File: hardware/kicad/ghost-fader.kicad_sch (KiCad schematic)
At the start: 0 parts

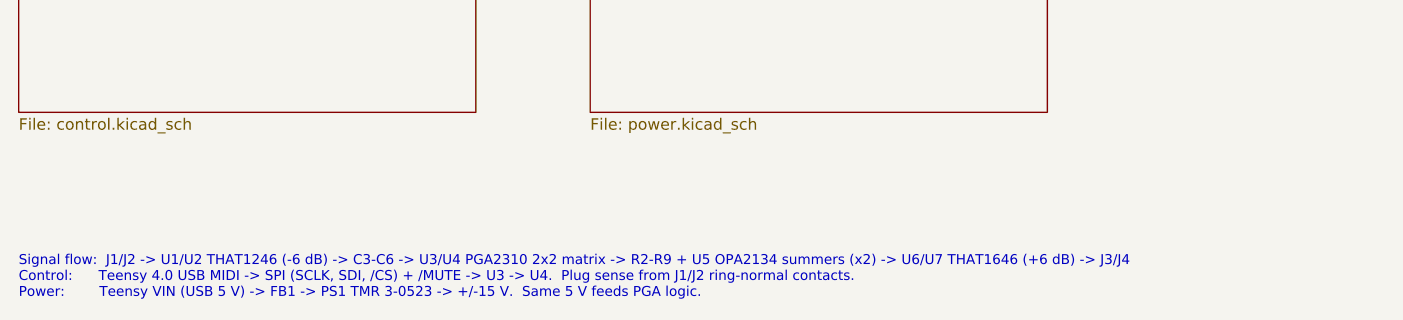
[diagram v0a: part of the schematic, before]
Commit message: Rev C: XIAO RP2040 and Traco TBA 2-0522 replace the Teensy 4.0 and TMR 3
Tier 1 cost-down, no change to the audio path. U9 becomes a Seeed XIAO
RP2040 on header pins (USB-C, TinyUSB MIDI, its 5V pin is VBUS straight
through), PS1 becomes a 2 W unregulated Traco TBA 2-0522 on KiCad's stock
SIP-7 footprint. Rails are now +/-12 V: the +/-15 V TBA 2-0523 would pass
the PGA2310's 16 V absolute maximum at light load. Parts cost drops from
about $145 to about $110.

- gen.py: TBA2_Dual and XIAO_RP2040 symbols, XIAO footprint (Seeed pin
  numbering, USB-C overhang drawn), control sheet rewired to D0-D10,
  power sheet and notes for the unregulated converter, +/-12V rails.
- check.py: new U9 / PS1 pins; NETLIST OK. ERC 0/0.
- Both boards rebuilt and re-routed (Freerouting 1.9), DRC 0 errors; the
  only warnings are jack-nose and USB-C shell silk over the board edge.
- Gerbers, drill, zips, BOM, schematic SVG/PDF and board renders
  regenerated. README and site updated: pin map, power budget
  (~250 mA typical), level budget at +/-12 V, parts list and totals.

Co-Authored-By: Claude Fable 5.1 <noreply@anthropic.com>
Claude-Session: https://claude.ai/code/session_01C8uqpe49go1TPWMsWKKVkn
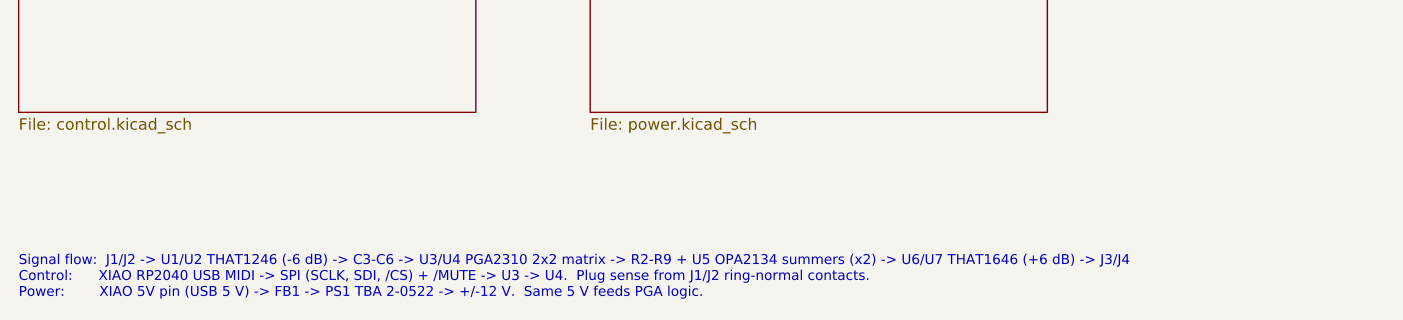
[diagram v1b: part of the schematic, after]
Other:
- note added: "Signal flow: J1/J2 -> U1/U2 THAT1246 (-6 dB) -> C3-C6 -> U3/U4 PGA2310 2x2 matrix -> R2-R9 + U5 OPA2134 summers (x2) -> U6/U7 THAT1646 (+6 dB) -> J3/J4 Control: XIAO RP2040 USB MIDI -> SPI (SCLK, SDI, /CS) + /MUTE -> U3 -> U4. Plug sense from J1/J2 ring-normal contacts. Power: XIAO 5V pin (USB 5 V) -> FB1 -> PS1 TBA 2-0522 -> +/-12 V. Same 5 V feeds PGA logic."
- note removed: "Signal flow: J1/J2 -> U1/U2 THAT1246 (-6 dB) -> C3-C6 -> U3/U4 PGA2310 2x2 matrix -> R2-R9 + U5 OPA2134 summers (x2) -> U6/U7 THAT1646 (+6 dB) -> J3/J4 Control: Teensy 4.0 USB MIDI -> SPI (SCLK, SDI, /CS) + /MUTE -> U3 -> U4. Plug sense from J1/J2 ring-normal contacts. Power: Teensy VIN (USB 5 V) -> FB1 -> PS1 TMR 3-0523 -> +/-15 V. Same 5 V feeds PGA logic."
- title: Ghost Fader - Rev B -> Ghost Fader - Rev C
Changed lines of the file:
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@@
 (kicad_sch (version 20250114) (generator "ghost-fader-gen") (generator_version "9.0") (paper "A4")
-  (title_block (title "Ghost Fader - Rev B") (date "2026-09-06") (rev "B") (company "Ghost Fader") (comment 1 "USB-MIDI volume and pan for two balanced line channels") (comment 2 "https://chris-albert.github.io/ghost-fader/"))
+  (title_block (title "Ghost Fader - Rev C") (date "2026-09-08") (rev "C") (company "Ghost Fader") (comment 1 "USB-MIDI volume and pan for two balanced line channels") (comment 2 "https://chris-albert.github.io/ghost-fader/"))
   (text "Ghost Fader" (exclude_from_sim no) (at 25.4 33.02 0) (effects (font (size 3.5 3.5)) (justify left bottom)))
   (text "USB-MIDI-controlled volume and pan for two balanced 1/4\" line channels. Bus powered, no external supply.\nSheets: 1 input, 2 matrix, 3 output, 4 control, 5 power. Nets between sheets are global labels; rails are power symbols." (exclude_from_sim no) (at 25.4 40.64 0) (effects (font (size 1.27 1.27)) (justify left bottom)))
@@
     (property "Sheetname" "Balanced inputs" (at 25.4 55.18 0) (effects (font (size 1.27 1.27)) (justify left bottom)))
     (property "Sheetfile" "input.kicad_sch" (at 25.4 76.8 0) (effects (font (size 1.27 1.27)) (justify left top)))
-    (instances (project "ghost-fader" (path "/fea7b9ca-c814-4436-8b9b-27ea79511ff8" (page "2"))))
+    (instances (project "ghost-fader" (path "/4c5c562c-d270-4690-8736-07f5ac58d31a" (page "2"))))
   )
   (sheet (at 88.9 55.88) (size 50.8 20.32) (exclude_from_sim no) (in_bom yes) (on_board yes) (dnp no) (fields_autoplaced yes) (stroke (width 0.1524) (type solid)) (fill (color 0 0 0 0.0000))
     (property "Sheetname" "2x2 gain matrix and summers" (at 88.9 55.18 0) (effects (font (size 1.27 1.27)) (justify left bottom)))
     (property "Sheetfile" "matrix.kicad_sch" (at 88.9 76.8 0) (effects (font (size 1.27 1.27)) (justify left top)))
-    (instances (project "ghost-fader" (path "/fea7b9ca-c814-4436-8b9b-27ea79511ff8" (page "3"))))
+    (instances (project "ghost-fader" (path "/4c5c562c-d270-4690-8736-07f5ac58d31a" (page "3"))))
   )
   (sheet (at 152.4 55.88) (size 50.8 20.32) (exclude_from_sim no) (in_bom yes) (on_board yes) (dnp no) (fields_autoplaced yes) (stroke (width 0.1524) (type solid)) (fill (color 0 0 0 0.0000))
     (property "Sheetname" "Balanced outputs" (at 152.4 55.18 0) (effects (font (size 1.27 1.27)) (justify left bottom)))
     (property "Sheetfile" "output.kicad_sch" (at 152.4 76.8 0) (effects (font (size 1.27 1.27)) (justify left top)))
-    (instances (project "ghost-fader" (path "/fea7b9ca-c814-4436-8b9b-27ea79511ff8" (page "4"))))
+    (instances (project "ghost-fader" (path "/4c5c562c-d270-4690-8736-07f5ac58d31a" (page "4"))))
   )
   (sheet (at 25.4 88.9) (size 50.8 20.32) (exclude_from_sim no) (in_bom yes) (on_board yes) (dnp no) (fields_autoplaced yes) (stroke (width 0.1524) (type solid)) (fill (color 0 0 0 0.0000))
     (property "Sheetname" "Control" (at 25.4 88.2 0) (effects (font (size 1.27 1.27)) (justify left bottom)))
     (property "Sheetfile" "control.kicad_sch" (at 25.4 109.82 0) (effects (font (size 1.27 1.27)) (justify left top)))
-    (instances (project "ghost-fader" (path "/fea7b9ca-c814-4436-8b9b-27ea79511ff8" (page "5"))))
+    (instances (project "ghost-fader" (path "/4c5c562c-d270-4690-8736-07f5ac58d31a" (page "5"))))
   )
   (sheet (at 88.9 88.9) (size 50.8 20.32) (exclude_from_sim no) (in_bom yes) (on_board yes) (dnp no) (fields_autoplaced yes) (stroke (width 0.1524) (type solid)) (fill (color 0 0 0 0.0000))
     (property "Sheetname" "Power" (at 88.9 88.2 0) (effects (font (size 1.27 1.27)) (justify left bottom)))
     (property "Sheetfile" "power.kicad_sch" (at 88.9 109.82 0) (effects (font (size 1.27 1.27)) (justify left top)))
-    (instances (project "ghost-fader" (path "/fea7b9ca-c814-4436-8b9b-27ea79511ff8" (page "6"))))
+    (instances (project "ghost-fader" (path "/4c5c562c-d270-4690-8736-07f5ac58d31a" (page "6"))))
   )
-  (text "Signal flow:  J1/J2 -> U1/U2 THAT1246 (-6 dB) -> C3-C6 -> U3/U4 PGA2310 2x2 matrix -> R2-R9 + U5 OPA2134 summers (x2) -> U6/U7 THAT1646 (+6 dB) -> J3/J4\nControl:      Teensy 4.0 USB MIDI -> SPI (SCLK, SDI, /CS) + /MUTE -> U3 -> U4.  Plug sense from J1/J2 ring-normal contacts.\nPower:        Teensy VIN (USB 5 V) -> FB1 -> PS1 TMR 3-0523 -> +/-15 V.  Same 5 V feeds PGA logic." (exclude_from_sim no) (at 25.4 130 0) (effects (font (size 1.1 1.1)) (justify left bottom)))
+  (text "Signal flow:  J1/J2 -> U1/U2 THAT1246 (-6 dB) -> C3-C6 -> U3/U4 PGA2310 2x2 matrix -> R2-R9 + U5 OPA2134 summers (x2) -> U6/U7 THAT1646 (+6 dB) -> J3/J4\nControl:      XIAO RP2040 USB MIDI -> SPI (SCLK, SDI, /CS) + /MUTE -> U3 -> U4.  Plug sense from J1/J2 ring-normal contacts.\nPower:        XIAO 5V pin (USB 5 V) -> FB1 -> PS1 TBA 2-0522 -> +/-12 V.  Same 5 V feeds PGA logic." (exclude_from_sim no) (at 25.4 130 0) (effects (font (size 1.1 1.1)) (justify left bottom)))
   (sheet_instances (path "/" (page "1")))
 )

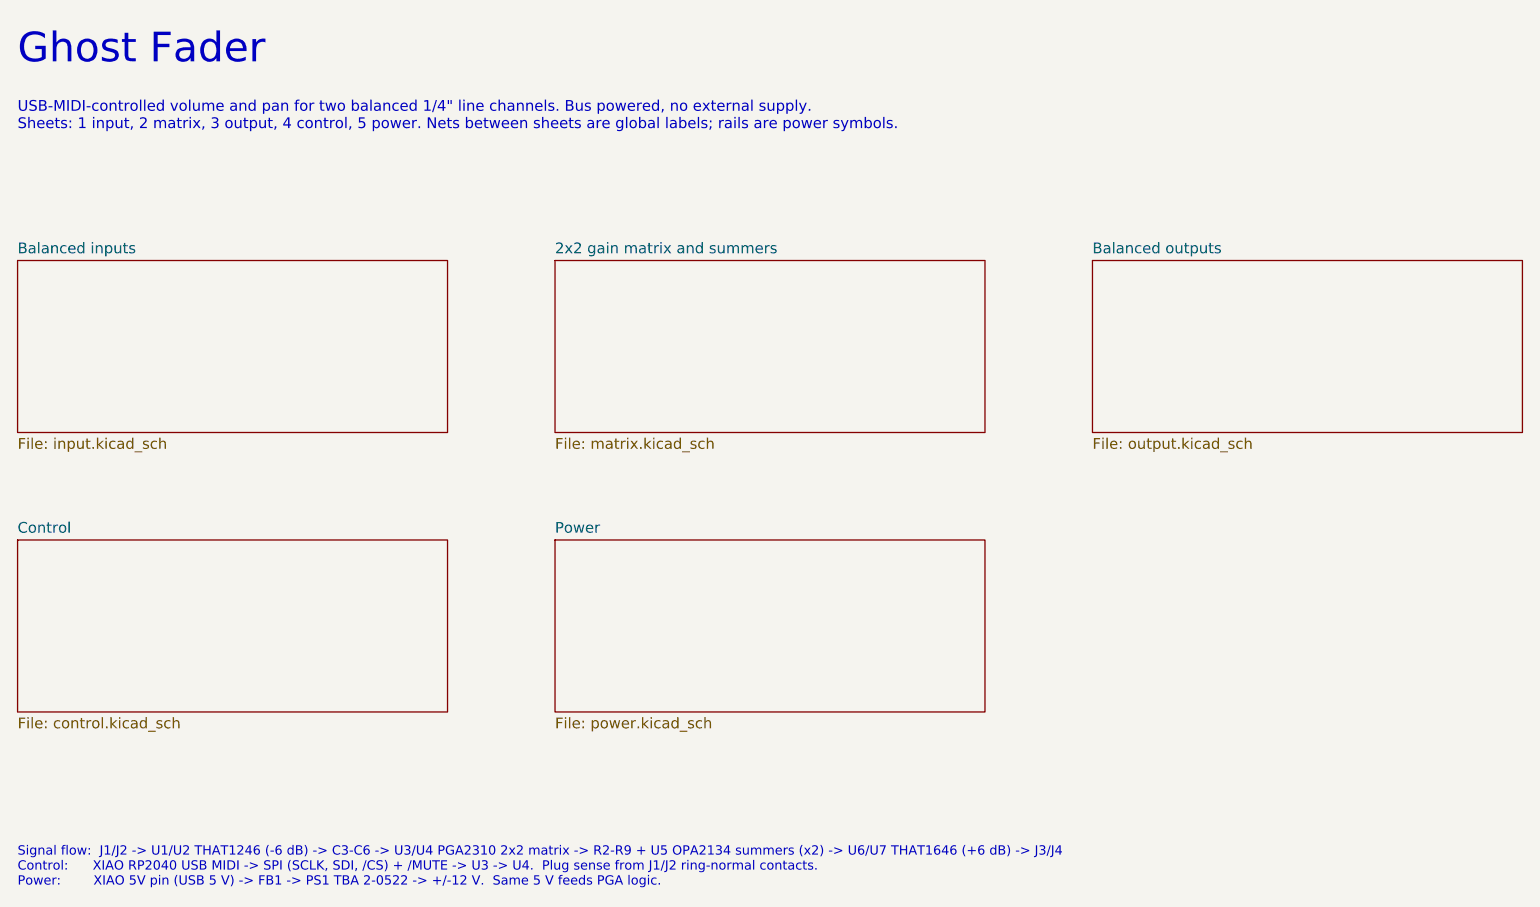
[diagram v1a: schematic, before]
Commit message: Rev D: isolate the audio ground from USB
Add a TI ISO7762FDW digital isolator on the four control lines and two
plug-sense lines, a 78L05 that makes +5VA from +12 V for the PGA logic
and the isolator's audio side, and a split ground: GND_USB (XIAO, USB-C,
switch, LED, ferrite, reservoir, DC-DC input) and GND (everything audio).
The two meet only through C45 (1 nF) and R17 (1 M) at PS1. The sense
pull-ups drop from 1 M to 100 k for the isolator's input leakage.

Both boards get two ground pours per layer with a 2 mm copper-free gap
and a rule area that keeps the router out; U8 and PS1 straddle the gap.
The 1590BB board's island is the front-left corner; the narrow board's
is a pocket under the XIAO with the audio ground wrapping beneath it.
ERC 0, netlist checked (61 nets, 263 pins), DRC clean on both routed
boards, and a script check confirms no copper crosses the gap.

README, docs page, schematic exports, renders, gerbers and BOM regenerated.

Co-Authored-By: Claude Fable 5.1 <noreply@anthropic.com>
Claude-Session: https://claude.ai/code/session_013C8baRPktSQjwfdzSRwmAq
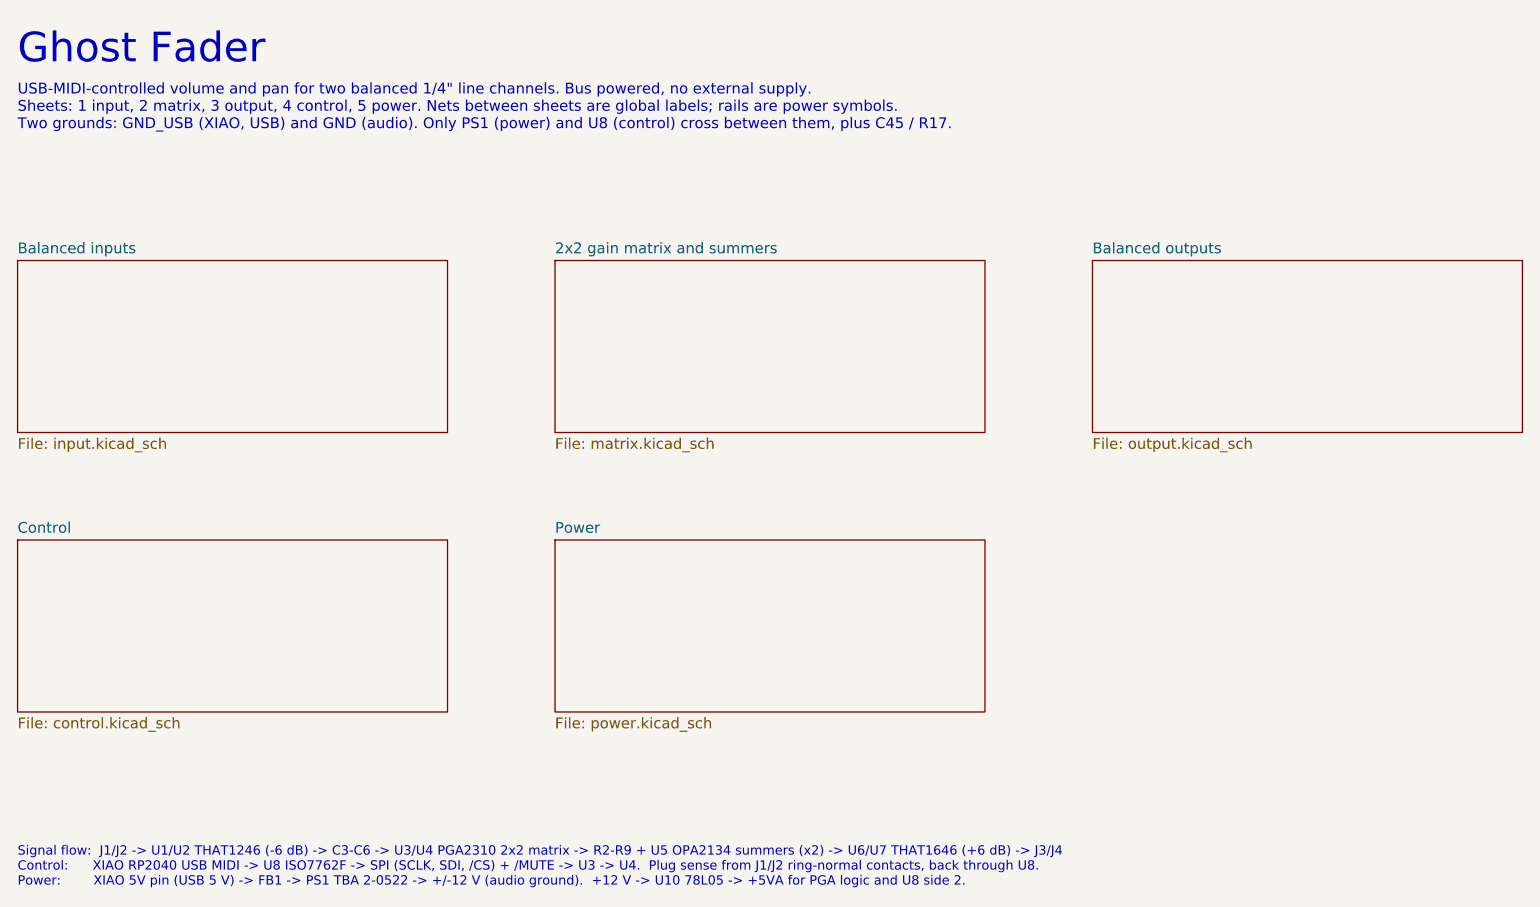
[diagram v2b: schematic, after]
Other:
- note added: "Signal flow: J1/J2 -> U1/U2 THAT1246 (-6 dB) -> C3-C6 -> U3/U4 PGA2310 2x2 matrix -> R2-R9 + U5 OPA2134 summers (x2) -> U6/U7 THAT1646 (+6 dB) -> J3/J4 Control: XIAO RP2040 USB MIDI -> U8 ISO7762F -> SPI (SCLK, SDI, /CS) + /MUTE -> U3 -> U4. Plug sense from J1/J2 ring-normal contacts, back through U8. Power: XIAO 5V pin (USB 5 V) -> FB1 -> PS1 TBA 2-0522 -> +/-12 V (audio ground). +12 V -> U10 78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"
- note added: "USB-MIDI-controlled volume and pan for two balanced 1/4" line channels. Bus powered, no external supply. Sheets: 1 input, 2 matrix, 3 output, 4 control, 5 power. Nets between sheets are global labels; rails are power symbols. Two grounds: GND_USB (XIAO, USB) and GND (audio). Only PS1 (power) and U8 (control) cross between them, plus C45 / R17."
- note removed: "Signal flow: J1/J2 -> U1/U2 THAT1246 (-6 dB) -> C3-C6 -> U3/U4 PGA2310 2x2 matrix -> R2-R9 + U5 OPA2134 summers (x2) -> U6/U7 THAT1646 (+6 dB) -> J3/J4 Control: XIAO RP2040 USB MIDI -> SPI (SCLK, SDI, /CS) + /MUTE -> U3 -> U4. Plug sense from J1/J2 ring-normal contacts. Power: XIAO 5V pin (USB 5 V) -> FB1 -> PS1 TBA 2-0522 -> +/-12 V. Same 5 V feeds PGA logic."
- note removed: "USB-MIDI-controlled volume and pan for two balanced 1/4" line channels. Bus powered, no external supply. Sheets: 1 input, 2 matrix, 3 output, 4 control, 5 power. Nets between sheets are global labels; rails are power symbols."
- title: Ghost Fader - Rev C -> Ghost Fader - Rev D
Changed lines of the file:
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@@
 (kicad_sch (version 20250114) (generator "ghost-fader-gen") (generator_version "9.0") (paper "A4")
-  (title_block (title "Ghost Fader - Rev C") (date "2026-09-08") (rev "C") (company "Ghost Fader") (comment 1 "USB-MIDI volume and pan for two balanced line channels") (comment 2 "https://chris-albert.github.io/ghost-fader/"))
+  (title_block (title "Ghost Fader - Rev D") (date "2026-09-09") (rev "D") (company "Ghost Fader") (comment 1 "USB-MIDI volume and pan for two balanced line channels") (comment 2 "https://chris-albert.github.io/ghost-fader/"))
   (text "Ghost Fader" (exclude_from_sim no) (at 25.4 33.02 0) (effects (font (size 3.5 3.5)) (justify left bottom)))
-  (text "USB-MIDI-controlled volume and pan for two balanced 1/4\" line channels. Bus powered, no external supply.\nSheets: 1 input, 2 matrix, 3 output, 4 control, 5 power. Nets between sheets are global labels; rails are power symbols." (exclude_from_sim no) (at 25.4 40.64 0) (effects (font (size 1.27 1.27)) (justify left bottom)))
+  (text "USB-MIDI-controlled volume and pan for two balanced 1/4\" line channels. Bus powered, no external supply.\nSheets: 1 input, 2 matrix, 3 output, 4 control, 5 power. Nets between sheets are global labels; rails are power symbols.\nTwo grounds: GND_USB (XIAO, USB) and GND (audio). Only PS1 (power) and U8 (control) cross between them, plus C45 / R17." (exclude_from_sim no) (at 25.4 40.64 0) (effects (font (size 1.27 1.27)) (justify left bottom)))
   (sheet (at 25.4 55.88) (size 50.8 20.32) (exclude_from_sim no) (in_bom yes) (on_board yes) (dnp no) (fields_autoplaced yes) (stroke (width 0.1524) (type solid)) (fill (color 0 0 0 0.0000))
     (property "Sheetname" "Balanced inputs" (at 25.4 55.18 0) (effects (font (size 1.27 1.27)) (justify left bottom)))
     (property "Sheetfile" "input.kicad_sch" (at 25.4 76.8 0) (effects (font (size 1.27 1.27)) (justify left top)))
-    (instances (project "ghost-fader" (path "/4c5c562c-d270-4690-8736-07f5ac58d31a" (page "2"))))
+    (instances (project "ghost-fader" (path "/ff864ed0-13b7-4c46-a78e-2ff7ed2b1e14" (page "2"))))
   )
   (sheet (at 88.9 55.88) (size 50.8 20.32) (exclude_from_sim no) (in_bom yes) (on_board yes) (dnp no) (fields_autoplaced yes) (stroke (width 0.1524) (type solid)) (fill (color 0 0 0 0.0000))
     (property "Sheetname" "2x2 gain matrix and summers" (at 88.9 55.18 0) (effects (font (size 1.27 1.27)) (justify left bottom)))
     (property "Sheetfile" "matrix.kicad_sch" (at 88.9 76.8 0) (effects (font (size 1.27 1.27)) (justify left top)))
-    (instances (project "ghost-fader" (path "/4c5c562c-d270-4690-8736-07f5ac58d31a" (page "3"))))
+    (instances (project "ghost-fader" (path "/ff864ed0-13b7-4c46-a78e-2ff7ed2b1e14" (page "3"))))
   )
   (sheet (at 152.4 55.88) (size 50.8 20.32) (exclude_from_sim no) (in_bom yes) (on_board yes) (dnp no) (fields_autoplaced yes) (stroke (width 0.1524) (type solid)) (fill (color 0 0 0 0.0000))
     (property "Sheetname" "Balanced outputs" (at 152.4 55.18 0) (effects (font (size 1.27 1.27)) (justify left bottom)))
     (property "Sheetfile" "output.kicad_sch" (at 152.4 76.8 0) (effects (font (size 1.27 1.27)) (justify left top)))
-    (instances (project "ghost-fader" (path "/4c5c562c-d270-4690-8736-07f5ac58d31a" (page "4"))))
+    (instances (project "ghost-fader" (path "/ff864ed0-13b7-4c46-a78e-2ff7ed2b1e14" (page "4"))))
   )
   (sheet (at 25.4 88.9) (size 50.8 20.32) (exclude_from_sim no) (in_bom yes) (on_board yes) (dnp no) (fields_autoplaced yes) (stroke (width 0.1524) (type solid)) (fill (color 0 0 0 0.0000))
     (property "Sheetname" "Control" (at 25.4 88.2 0) (effects (font (size 1.27 1.27)) (justify left bottom)))
     (property "Sheetfile" "control.kicad_sch" (at 25.4 109.82 0) (effects (font (size 1.27 1.27)) (justify left top)))
-    (instances (project "ghost-fader" (path "/4c5c562c-d270-4690-8736-07f5ac58d31a" (page "5"))))
+    (instances (project "ghost-fader" (path "/ff864ed0-13b7-4c46-a78e-2ff7ed2b1e14" (page "5"))))
   )
   (sheet (at 88.9 88.9) (size 50.8 20.32) (exclude_from_sim no) (in_bom yes) (on_board yes) (dnp no) (fields_autoplaced yes) (stroke (width 0.1524) (type solid)) (fill (color 0 0 0 0.0000))
     (property "Sheetname" "Power" (at 88.9 88.2 0) (effects (font (size 1.27 1.27)) (justify left bottom)))
     (property "Sheetfile" "power.kicad_sch" (at 88.9 109.82 0) (effects (font (size 1.27 1.27)) (justify left top)))
-    (instances (project "ghost-fader" (path "/4c5c562c-d270-4690-8736-07f5ac58d31a" (page "6"))))
+    (instances (project "ghost-fader" (path "/ff864ed0-13b7-4c46-a78e-2ff7ed2b1e14" (page "6"))))
   )
-  (text "Signal flow:  J1/J2 -> U1/U2 THAT1246 (-6 dB) -> C3-C6 -> U3/U4 PGA2310 2x2 matrix -> R2-R9 + U5 OPA2134 summers (x2) -> U6/U7 THAT1646 (+6 dB) -> J3/J4\nControl:      XIAO RP2040 USB MIDI -> SPI (SCLK, SDI, /CS) + /MUTE -> U3 -> U4.  Plug sense from J1/J2 ring-normal contacts.\nPower:        XIAO 5V pin (USB 5 V) -> FB1 -> PS1 TBA 2-0522 -> +/-12 V.  Same 5 V feeds PGA logic." (exclude_from_sim no) (at 25.4 130 0) (effects (font (size 1.1 1.1)) (justify left bottom)))
+  (text "Signal flow:  J1/J2 -> U1/U2 THAT1246 (-6 dB) -> C3-C6 -> U3/U4 PGA2310 2x2 matrix -> R2-R9 + U5 OPA2134 summers (x2) -> U6/U7 THAT1646 (+6 dB) -> J3/J4\nControl:      XIAO RP2040 USB MIDI -> U8 ISO7762F -> SPI (SCLK, SDI, /CS) + /MUTE -> U3 -> U4.  Plug sense from J1/J2 ring-normal contacts, back through U8.\nPower:        XIAO 5V pin (USB 5 V) -> FB1 -> PS1 TBA 2-0522 -> +/-12 V (audio ground).  +12 V -> U10 78L05 -> +5VA for PGA logic and U8 side 2." (exclude_from_sim no) (at 25.4 130 0) (effects (font (size 1.1 1.1)) (justify left bottom)))
   (sheet_instances (path "/" (page "1")))
 )
